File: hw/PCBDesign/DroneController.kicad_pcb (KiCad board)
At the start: 2 copper layers, 180 parts, among them J1 SerialDebug, J10 Conn_01x03, J11 Conn_01x03, J12 Conn_01x03, J13 Conn_01x03, J14 Conn_01x03, J2 USB_B_Micro, J3 ExtBatt, J4 Conn_ARM_JTAG_SWD_10, J5 EncoderConn, J6 JoystickConn, J7 Conn_01x03, J8 Conn_01x03, J9 Conn_01x03, Q1 MMBT3904, SW13 Key_User, SW15 Key_nRESET, SW17 Key_nBOOT, U1 74HC165, U10 AMS1117-3.3, U11 74HC595, U12 74HC595, U13 STM32F446RETx, U2 74HC165, U3 74HC165, U4 AT25SF081, U5 AT24C256, U6 NRF24L01_Breakout, U7 BQ24074RGT, U8 AMS1117-3.3, U9 AMS1117-3.3, Y1 8MHz Crystal

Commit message: Update pcb
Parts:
- added H1: MountingHole_Pad, MountingHole:MountingHole_3.2mm_M3_Pad_Via, F.Cu at (113.8, 83.8)
- added H2: MountingHole_Pad, MountingHole:MountingHole_3.2mm_M3_Pad_Via, F.Cu at (113.8, 126.0)
- added H3: MountingHole_Pad, MountingHole:MountingHole_3.2mm_M3_Pad_Via, F.Cu at (206.2, 83.8)
- added H4: MountingHole_Pad, MountingHole:MountingHole_3.2mm_M3_Pad_Via, F.Cu at (206.2, 126.0)
- J10, J11, J12, J13, J14, J5, J6, J7, J8, J9: moved to B.Cu
- moved D4 201.3 mm to (206.0, 97.8), turned to 180 degrees
- moved J10 193.1 mm to (170.8, 34.8)
- moved J11 193.1 mm to (195.3, 34.8)
- moved J13 193.1 mm to (183.0, 34.8)
- moved J8 193.1 mm to (158.5, 34.8)
- moved U6 191.0 mm to (155.0, 127.0), turned to 90 degrees
- moved SW15 189.9 mm to (205.7, 117.3)
- moved SW17 189.6 mm to (205.7, 111.8)
- moved D3 188.0 mm to (206.0, 100.3), turned to 180 degrees
- moved D5 183.6 mm to (206.0, 95.2), turned to 180 degrees
- moved D6 181.6 mm to (206.0, 92.7), turned to 180 degrees
- moved SW13 181.4 mm to (205.7, 106.2)
- moved J7 172.2 mm to (131.0, 49.0)
- moved J3 170.8 mm to (129.5, 86.4)
- moved J2 164.8 mm to (112.0, 105.0), turned to 270 degrees
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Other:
- board outline added: 100 x 50 mm

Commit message: Laid out power section
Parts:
- added R52: 33, Resistor_SMD:R_0402_1005Metric, F.Cu at (183.7, 148.6)
- added R54: 33, Resistor_SMD:R_0402_1005Metric, F.Cu at (186.6, 148.6)
- J10: value Conn_01x03 -> SW_B
- J11: value Conn_01x03 -> YTrim; moved to F.Cu
- J12: value Conn_01x03 -> SW_C
- J13: value Conn_01x03 -> TTrim; moved to F.Cu
- J14: value Conn_01x03 -> SW_D
- J6: moved to F.Cu
- J7: value Conn_01x03 -> PTrim; moved to F.Cu
- J8: value Conn_01x03 -> SW_A
- J9: value Conn_01x03 -> RTrim; moved to F.Cu
- moved U1 310.6 mm to (271.6, 106.4)
- moved U2 291.2 mm to (257.6, 119.2)
- moved U3 271.8 mm to (249.0, 106.4)
- moved C1 266.9 mm to (232.4, 116.5)
- moved C2 266.9 mm to (235.2, 116.5)
- moved R2 266.9 mm to (226.6, 118.5)
- moved R45 266.9 mm to (229.5, 118.5)
- moved R46 266.9 mm to (229.5, 116.5)
- moved R47 266.9 mm to (223.7, 118.5)
- moved R49 266.9 mm to (226.6, 116.5)
- moved R51 266.9 mm to (223.7, 116.5)
- moved C3 238.7 mm to (219.4, 109.6)
- moved R1 238.7 mm to (219.4, 107.6)
- moved C50 221.0 mm to (248.0, 95.6)
- moved Q1 221.0 mm to (223.3, 108.5)
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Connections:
- net Net-(C39-Pad1) renamed /Power Supply/VBattProtectOut
- R73 pad 2: +3V3 -> /Power Supply/vBatt
- R82 pad 2: +3V3 -> /Power Supply/vBatt
- R83 pad 2: +3V3 -> /Power Supply/vBatt
- U13 pad 44: /Power Supply/USB_D- -> Net-(R52-Pad2)
- U13 pad 45: /Power Supply/USB_D+ -> Net-(R54-Pad2)
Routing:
- net GND: track 0.00 -> 51.3 mm, vias 0 -> 26
- net /Power Supply/USB_D-: track 0.00 -> 26.3 mm
- net /Power Supply/USB_D+: track 0.00 -> 26.1 mm
- net /Power Supply/vBatt: track 0.00 -> 20.5 mm
- net /Power Supply/VBattProtectOut: track 0.00 -> 12.0 mm, vias 0 -> 13
- net nBatteryChargeGood: track 0.00 -> 11.1 mm, vias 0 -> 2
- net +5V: track 0.00 -> 10.5 mm
- net nBatteryPowerGood: track 0.00 -> 9.02 mm, vias 0 -> 1
- net /Power Supply/CHG_nEN: track 0.00 -> 8.27 mm, vias 0 -> 1
- net +3.3VP: track 0.00 -> 6.57 mm
- net +3V3: track 0.00 -> 6.54 mm, vias 0 -> 6
- net +3.3VADC: track 0.00 -> 6.54 mm, vias 0 -> 6
- net /Processor/BattChgCfg0: track 0.00 -> 3.47 mm, vias 0 -> 1
- net Net-(R72-Pad1): track 0.00 -> 3.14 mm
- net Net-(R78-Pad1): track 0.00 -> 2.73 mm
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- added copper zone on F.Cu, net +3.3VADC
- added copper zone on F.Cu, net +3V3
- added copper zone on F.Cu, net /Power Supply/VBattProtectOut
- added copper zone on In2.Cu, net /Power Supply/VBattProtectOut
- added copper zone on In1.Cu, net GND
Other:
- copper layers 2 -> 4
- net class Default: via_dia 0.8 -> 0.4; via_drill 0.4 -> 0.3
- board text added: "DN"
- board text added: "GND"
- board text added: "HM-BT4052"
- board text added: "INT"
- board text added: "PDN"
- board text added: "RXD"
- board text added: "TXD"
- board text added: "VDD"
- board text added: "WKUP"

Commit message: Lay out more PCB
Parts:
- removed C42, C43, C45, C46: 1uF, Capacitor_SMD:C_0805_2012Metric
- removed C48, C49: 100n, Capacitor_SMD:C_0402_1005Metric
- removed R86, R87: 10k, Resistor_SMD:R_0402_1005Metric
- removed U10, U9: AMS1117-3.3, Package_TO_SOT_SMD:SOT-223-3_TabPin2
- added C26: 100n, Capacitor_SMD:C_0402_1005Metric, F.Cu at (157.3, 103.2)
- added C27: 100n, Capacitor_SMD:C_0402_1005Metric, F.Cu at (155.0, 110.1)
- added C29: 100n, Capacitor_SMD:C_0402_1005Metric, F.Cu at (168.3, 119.2)
- added C31: 100n, Capacitor_SMD:C_0402_1005Metric, F.Cu at (171.7, 119.2)
- added C33: 100n, Capacitor_SMD:C_0402_1005Metric, F.Cu at (161.7, 110.0)
- added C55: 100n, Capacitor_SMD:C_0402_1005Metric, F.Cu at (169.8, 101.5)
- added C56: 100n, Capacitor_SMD:C_0402_1005Metric, F.Cu at (178.8, 109.1)
- added C57: 100n, Capacitor_SMD:C_0402_1005Metric, F.Cu at (176.9, 114.5)
- added C58: 100n, Capacitor_SMD:C_0402_1005Metric, F.Cu at (200.8, 116.6)
- added C59: 10uF, Capacitor_SMD:C_0805_2012Metric, F.Cu at (203.1, 116.6)
- added D7: BT_ON, LED_SMD:LED_0603_1608Metric, F.Cu at (206.6, 116.6)
- added Q2: si2302, Package_TO_SOT_SMD:SOT-23, F.Cu at (203.1, 119.3)
- added Q3: si2302, Package_TO_SOT_SMD:SOT-23, F.Cu at (182.4, 116.9)
- added Q4: si2301, Package_TO_SOT_SMD:SOT-23, F.Cu at (206.5, 119.3)
- added Q5: si2301, Package_TO_SOT_SMD:SOT-23, F.Cu at (185.8, 116.9)
- added R100: 10k, Resistor_SMD:R_0402_1005Metric, F.Cu at (199.7, 116.6)
- added R101: 560, Resistor_SMD:R_0402_1005Metric, F.Cu at (208.9, 116.5)
- added R56: 10k, Resistor_SMD:R_0402_1005Metric, F.Cu at (200.8, 119.3)
- added R58: 10k, Resistor_SMD:R_0402_1005Metric, F.Cu at (180.2, 116.9)
- added R59: 10k, Resistor_SMD:R_0402_1005Metric, F.Cu at (208.9, 119.2)
- added R98: 10k, Resistor_SMD:R_0402_1005Metric, F.Cu at (188.0, 116.9)
- added R99: 10k, Resistor_SMD:R_0402_1005Metric, F.Cu at (147.6, 103.2)
- added U14: RN4871, RF_Module:Microchip_RN4871, F.Cu at (201.1, 110.0)
- moved U1 135.8 mm to (136.0, 99.8), turned to 90 degrees
- moved R67 103.2 mm to (147.6, 104.4)
- moved R92 100.9 mm to (162.9, 141.3)
- moved R61 97.1 mm to (147.3, 114.8), turned to 180 degrees
- moved U4 95.9 mm to (152.4, 105.5)
- moved R62 94.8 mm to (147.3, 112.6)
- moved R60 94.5 mm to (147.3, 115.9)
- moved C23 92.7 mm to (157.0, 94.4)
- moved R65 92.3 mm to (147.3, 111.5)
- moved R63 92.3 mm to (147.3, 113.7), turned to 180 degrees
- moved R68 90.5 mm to (157.8, 112.1), turned to 270 degrees
- moved R66 89.9 mm to (147.3, 110.4), turned to 180 degrees
- moved R69 89.3 mm to (156.7, 112.1), turned to 270 degrees
- moved R95 87.7 mm to (169.6, 140.9)
- moved R97 87.0 mm to (170.6, 119.2), turned to 270 degrees
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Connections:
- C34 pad 1: +3.3VP -> Net-(C34-Pad1)
- C35 pad 1: +3.3VP -> Net-(C34-Pad1)
- J2 pad 4: Net-(J2-Pad4) -> (no net)
- J4 pad 7: Net-(J4-Pad7) -> (no net)
- R13 pad 1: /Human Machine Interface/d1 -> (no net)
- R14 pad 1: /Human Machine Interface/d0 -> (no net)
- R16 pad 2: /Human Machine Interface/d16 -> (no net)
- R18 pad 1: /Human Machine Interface/d8 -> (no net)
- R19 pad 2: /Human Machine Interface/d9 -> (no net)
- R2 pad 1: /Human Machine Interface/d23 -> (no net)
- R21 pad 2: /Human Machine Interface/d17 -> (no net)
- R25 pad 1: /Human Machine Interface/d10 -> (no net)
- R26 pad 2: /Human Machine Interface/d11 -> (no net)
- R27 pad 2: /Human Machine Interface/d18 -> (no net)
- R31 pad 1: /Human Machine Interface/d12 -> (no net)
- R32 pad 2: /Human Machine Interface/d13 -> (no net)
- R33 pad 2: /Human Machine Interface/d19 -> (no net)
- R37 pad 1: /Human Machine Interface/d14 -> (no net)
- R38 pad 2: /Human Machine Interface/d15 -> (no net)
- R45 pad 1: /Human Machine Interface/d22 -> (no net)
- R46 pad 1: /Human Machine Interface/d4 -> (no net)
- R47 pad 1: /Human Machine Interface/d5 -> (no net)
- R48 pad 2: /Human Machine Interface/d2 -> (no net)
- R49 pad 1: /Human Machine Interface/d6 -> (no net)
- R51 pad 1: /Human Machine Interface/d7 -> (no net)
- R55 pad 2: /Human Machine Interface/d3 -> (no net)
- R70 pad 1: +3.3VP -> Net-(C34-Pad1)
- R71 pad 1: +3.3VP -> Net-(C34-Pad1)
- U1 pad 11: /Human Machine Interface/d16 -> (no net)
- U1 pad 12: /Human Machine Interface/d17 -> (no net)
- U1 pad 13: /Human Machine Interface/d18 -> (no net)
- U1 pad 14: /Human Machine Interface/d19 -> (no net)
- U1 pad 3: nBatteryPowerGood -> (no net)
- U1 pad 4: nBatteryChargeGood -> (no net)
- U1 pad 5: /Human Machine Interface/d22 -> (no net)
- U1 pad 6: /Human Machine Interface/d23 -> (no net)
- U1 pad 7: Net-(U1-Pad7) -> (no net)
- U11 pad 1: /Processor/BattChgCfg1 -> (no net)
- U11 pad 15: /Processor/BattChgCfg0 -> (no net)
- U11 pad 2: /Power Supply/CHG_nEN -> (no net)
- U11 pad 3: /Processor/BT_nWakeup -> (no net)
- U11 pad 4: /Processor/BT_nPowerUp -> (no net)
- U11 pad 5: /Processor/BT_VCC_EN -> (no net)
- U11 pad 6: /Processor/RF24_VCC_EN -> (no net)
- U11 pad 9: Net-(U11-Pad9) -> (no net)
- U12 pad 1: Net-(U12-Pad1) -> (no net)
- U12 pad 15: Net-(U12-Pad15) -> (no net)
- U12 pad 2: Net-(U12-Pad2) -> (no net)
- U12 pad 3: Net-(U12-Pad3) -> (no net)
- U12 pad 9: Net-(U12-Pad9) -> (no net)
- U13 pad 13: +3.3VADC -> +3V3
- U13 pad 14: /Power Supply/V_Batt_Sense -> (no net)
- U13 pad 16: +3.3VP -> (no net)
- U13 pad 17: +3.3VADC -> (no net)
- U13 pad 2: Net-(U13-Pad2) -> (no net)
- U13 pad 28: Net-(U13-Pad28) -> (no net)
- U13 pad 3: Net-(U13-Pad3) -> (no net)
- U13 pad 39: /Wireless/BT_INT_REQ -> (no net)
- U13 pad 4: Net-(U13-Pad4) -> (no net)
- U13 pad 59: Net-(U13-Pad59) -> (no net)
- U2 pad 11: /Human Machine Interface/d8 -> (no net)
- U2 pad 12: /Human Machine Interface/d9 -> (no net)
- U2 pad 13: /Human Machine Interface/d10 -> (no net)
- U2 pad 14: /Human Machine Interface/d11 -> (no net)
- U2 pad 3: /Human Machine Interface/d12 -> (no net)
- U2 pad 4: /Human Machine Interface/d13 -> (no net)
- U2 pad 5: /Human Machine Interface/d14 -> (no net)
- U2 pad 6: /Human Machine Interface/d15 -> (no net)
- U2 pad 7: Net-(U2-Pad7) -> (no net)
- U3 pad 11: /Human Machine Interface/d0 -> (no net)
- U3 pad 12: /Human Machine Interface/d1 -> (no net)
- U3 pad 13: /Human Machine Interface/d2 -> (no net)
- U3 pad 14: /Human Machine Interface/d3 -> (no net)
- U3 pad 3: /Human Machine Interface/d4 -> (no net)
- U3 pad 4: /Human Machine Interface/d5 -> (no net)
- U3 pad 5: /Human Machine Interface/d6 -> (no net)
- U3 pad 6: /Human Machine Interface/d7 -> (no net)
- U3 pad 7: Net-(U3-Pad7) -> (no net)
- U6 pad 2: +3.3VP -> Net-(C34-Pad1)
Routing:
- net GND: track 51.3 -> 100.3 mm, vias 26 -> 68
- net +3V3: track 6.54 -> 54.3 mm, vias 6 -> 32
- net /Wireless/BT_TX: track 0.00 -> 33.3 mm, vias 0 -> 2
- net /Wireless/BT_RX: track 0.00 -> 32.3 mm, vias 0 -> 2
- net /Processor/RF24_nCS: track 0.00 -> 24.8 mm
- net /Processor/NOR_nCS: track 0.00 -> 23.8 mm, vias 0 -> 2
- net /Processor/NOR_MISO: track 0.00 -> 20.8 mm, vias 0 -> 2
- net /Processor/EEPROM_SDA: track 0.00 -> 20.5 mm, vias 0 -> 2
- net /Processor/EEPROM_SCL: track 0.00 -> 17.8 mm, vias 0 -> 2
- net /Human Machine Interface/ENC1_A: track 0.00 -> 17.7 mm
- net /Processor/RF24_nIRQ: track 0.00 -> 16.9 mm
- net /Human Machine Interface/ENC1_B: track 0.00 -> 16.2 mm
- net /Power Supply/USB_D+: track 26.1 -> 42.1 mm
- net /Power Supply/USB_D-: track 26.3 -> 42.2 mm
- net /Processor/NOR_SCK: track 0.00 -> 15.6 mm, vias 0 -> 2
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- added copper zone on In2.Cu, net +3V3
- removed copper zone on F.Cu, net +3.3VADC
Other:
- net class Default: clearance 0.2 -> 0.09
- rule trace_clearance: 0.2 -> 0.09
- board text removed: "DN"
- board text removed: "GND"
- board text removed: "HM-BT4052"
- board text removed: "INT"
- board text removed: "PDN"
- board text removed: "RXD"
- board text removed: "TXD"
- board text removed: "VDD"
- board text removed: "WKUP"

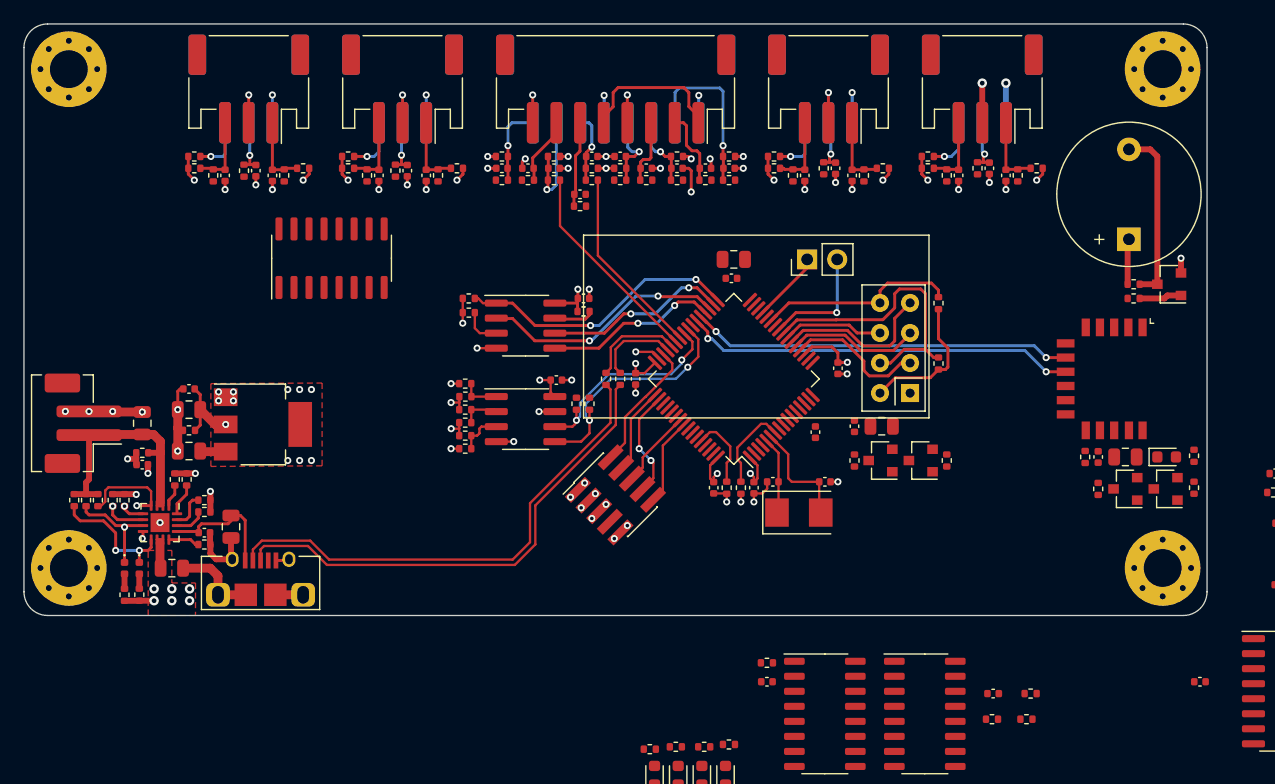
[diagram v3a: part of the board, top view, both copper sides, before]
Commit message: Routed most of the core peripherals
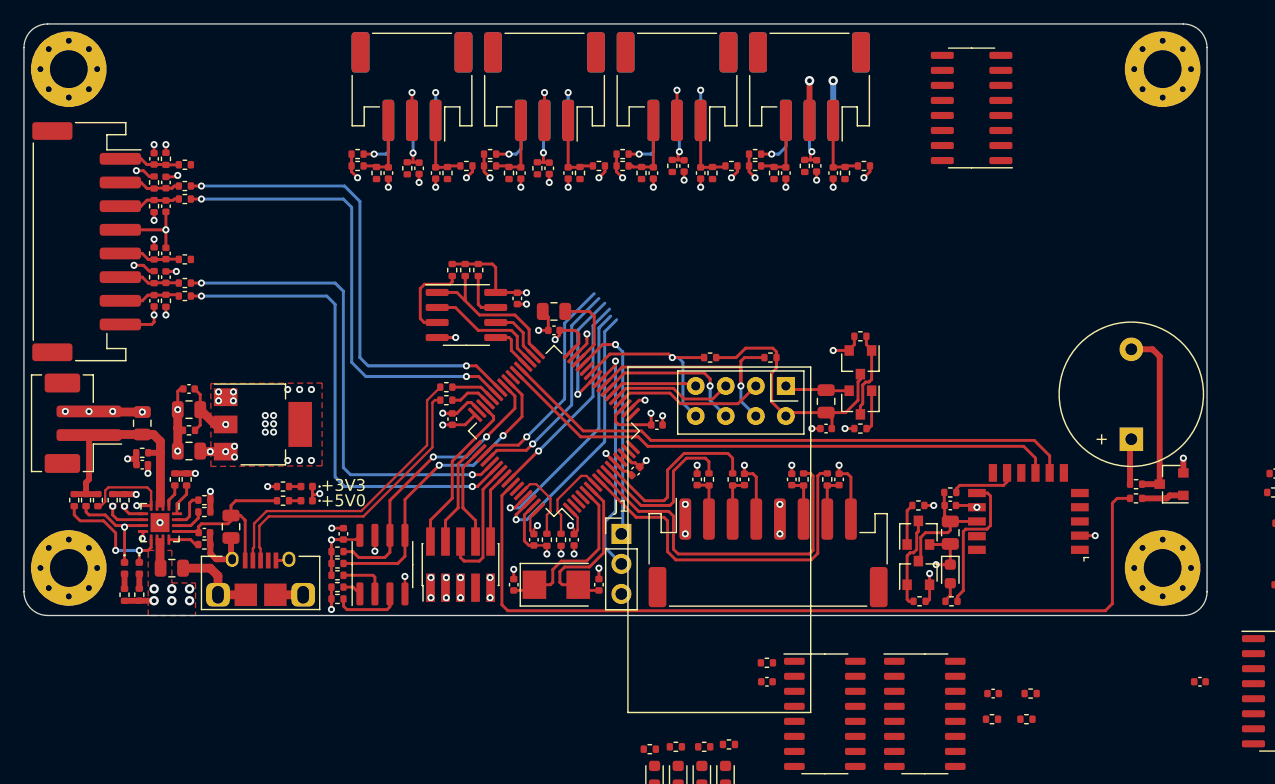
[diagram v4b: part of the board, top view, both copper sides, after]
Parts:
- removed R65: 10k, Resistor_SMD:R_0402_1005Metric
- added D8: LED_5V0, LED_SMD:LED_0402_1005Metric, F.Cu at (133.9, 120.3)
- added D9: LED_3V3, LED_SMD:LED_0402_1005Metric, F.Cu at (133.9, 119.1)
- J1: footprint Connector_PinHeader_2.54mm:PinHeader_1x02_P2.54mm_Vertical -> Connector_PinHeader_2.54mm:PinHeader_1x03_P2.54mm_Vertical
- J5: moved to F.Cu
- R60: value 10k -> 1.5k
- R63: value 10k -> 330
- moved U1 55.6 mm to (190.1, 87.1), turned to 180 degrees
- moved C7 49.9 mm to (121.0, 103.4), turned to 270 degrees
- moved R10 49.1 mm to (122.0, 103.4), turned to 270 degrees
- moved R6 47.0 mm to (123.6, 103.0)
- moved J5 46.6 mm to (115.3, 98.4), turned to 270 degrees
- moved R9 45.4 mm to (121.0, 101.4), turned to 270 degrees
- moved C6 44.2 mm to (122.0, 101.4), turned to 270 degrees
- moved R5 42.5 mm to (123.6, 101.9)
- moved J6 41.3 mm to (172.9, 124.7), turned to 0 degrees
- moved R12 40.1 mm to (121.0, 99.4), turned to 270 degrees
- moved C9 39.3 mm to (122.0, 99.4), turned to 90 degrees
- moved R14 37.4 mm to (123.6, 99.9), turned to 180 degrees
- moved C22 37.2 mm to (178.9, 118.5), turned to 90 degrees
- moved R8 37.1 mm to (121.0, 95.4), turned to 270 degrees
- moved C5 36.2 mm to (122.0, 95.4), turned to 270 degrees
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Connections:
- J6 pad 1: /Human Machine Interface/VAnalogRef -> +3V3
- J6 pad 5: /Human Machine Interface/VAnalogRef -> +3V3
- R60 pad 1: +3V3 -> Net-(D8-Pad2)
- R60 pad 2: Net-(R60-Pad2) -> +5V
- R61 pad 1: Net-(R60-Pad2) -> Net-(R61-Pad1)
- R63 pad 1: Net-(R62-Pad2) -> Net-(D9-Pad2)
- R63 pad 2: GND -> +3V3
- R66 pad 1: Net-(R65-Pad2) -> GND
- R66 pad 2: GND -> Net-(R66-Pad2)
- U13 pad 10: /Processor/ANALOG_IN_VYAW -> /Processor/ANALOG_IN_VTHROTTLE
- U13 pad 11: /Processor/ANALOG_IN_VTHROTTLE -> /Processor/ANALOG_IN_VYAW
- U13 pad 14: (no net) -> +3V3
- U13 pad 15: +3V3 -> (no net)
- U13 pad 42: /Human Machine Interface/ENC1_B -> /Human Machine Interface/ENC1_A
- U13 pad 43: /Human Machine Interface/ENC1_A -> /Human Machine Interface/ENC1_B
- U13 pad 53: /Human Machine Interface/ENC0_B -> /Human Machine Interface/ENC0_A
- U13 pad 54: /Human Machine Interface/ENC0_A -> /Human Machine Interface/ENC0_B
- U13 pad 8: /Processor/ANALOG_IN_VPITCH -> /Processor/ANALOG_IN_VROLL
- U13 pad 9: /Processor/ANALOG_IN_VROLL -> /Processor/ANALOG_IN_VPITCH
- U5 pad 1: Net-(R65-Pad2) -> Net-(R66-Pad2)
- U5 pad 3: Net-(R60-Pad2) -> Net-(R61-Pad1)
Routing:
- net /Human Machine Interface/PWM_Buzzer: track 0.00 -> 72.7 mm
- net /Human Machine Interface/ENC0_B: track 0.00 -> 41.7 mm, vias 0 -> 2
- net /Human Machine Interface/ENC0_A: track 0.00 -> 41.3 mm, vias 0 -> 2
- net GND: track 100.3 -> 139.3 mm, vias 68 -> 75
- net /Processor/ANALOG_IN_VROLL: track 0.00 -> 30.4 mm
- net /Processor/ANALOG_IN_VPITCH: track 0.00 -> 29.4 mm
- net /Human Machine Interface/ENC1_B: track 16.2 -> 40.3 mm, vias 0 -> 2
- net /Human Machine Interface/ENC1_A: track 17.7 -> 41.0 mm, vias 0 -> 2
- net /Human Machine Interface/KEY_nCS: track 0.00 -> 23.0 mm, vias 0 -> 1
- net /Human Machine Interface/KEY_nSAMPLE: track 0.00 -> 21.8 mm, vias 0 -> 1
- net +3V3: track 54.3 -> 74.0 mm, vias 32 -> 45
- net /Human Machine Interface/KEY_MISO: track 0.00 -> 19.0 mm, vias 0 -> 1
- net /Human Machine Interface/KEY_SCK: track 0.00 -> 18.8 mm, vias 0 -> 1
- net /Processor/KeyOut_nCS: track 0.00 -> 18.1 mm, vias 0 -> 1
- net /Power Supply/USB_D+: track 42.1 -> 24.9 mm
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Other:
- board text added: "+3V3"
- board text added: "+5V0"

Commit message: Complete route of draft #1 finished
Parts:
- removed C51: 100n, Capacitor_SMD:C_0402_1005Metric
- removed D3: DBG_LED_3, LED_SMD:LED_0603_1608Metric
- removed R89, R91: 10k, Resistor_SMD:R_0402_1005Metric
- removed R92: 560, Resistor_SMD:R_0402_1005Metric
- removed U12: 74HC595, Package_SO:SO-16_3.9x9.9mm_P1.27mm
- moved U3 93.5 mm to (131.0, 98.4)
- moved SW17 88.0 mm to (125.0, 84.0)
- moved C3 85.6 mm to (131.0, 92.7), turned to 180 degrees
- moved R57 83.2 mm to (124.0, 87.5)
- moved R55 82.2 mm to (126.0, 88.6)
- moved C32 80.8 mm to (126.0, 87.5), turned to 180 degrees
- moved SW13 80.0 mm to (132.0, 84.0)
- moved R1 77.7 mm to (130.9, 104.3), turned to 180 degrees
- moved R48 73.7 mm to (133.0, 88.6)
- moved R50 73.6 mm to (131.0, 87.5)
- moved C28 73.3 mm to (133.0, 87.5), turned to 180 degrees
- moved U2 68.0 mm to (154.0, 99.0), turned to 270 degrees
- moved R53 62.6 mm to (136.7, 112.0), turned to 90 degrees
- moved C2 62.1 mm to (159.8, 101.4), turned to 90 degrees
- moved D4 61.7 mm to (208.0, 99.0), turned to 180 degrees
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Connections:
- R13 pad 1: (no net) -> /Human Machine Interface/d6
- R14 pad 1: (no net) -> /Human Machine Interface/d7
- R16 pad 2: (no net) -> /Human Machine Interface/d23
- R18 pad 1: (no net) -> /Human Machine Interface/d14
- R19 pad 2: (no net) -> /Human Machine Interface/d12
- R2 pad 1: (no net) -> /Human Machine Interface/d17
- R21 pad 2: (no net) -> /Human Machine Interface/d9
- R25 pad 1: (no net) -> /Human Machine Interface/d3
- R26 pad 2: (no net) -> /Human Machine Interface/d15
- R27 pad 2: (no net) -> /Human Machine Interface/d13
- R31 pad 1: (no net) -> /Human Machine Interface/d8
- R32 pad 2: (no net) -> /Human Machine Interface/d10
- R33 pad 2: (no net) -> /Human Machine Interface/d2
- R37 pad 1: (no net) -> /Human Machine Interface/d11
- R38 pad 2: (no net) -> /Human Machine Interface/d22
- R45 pad 1: (no net) -> /Human Machine Interface/d21
- R46 pad 1: (no net) -> /Human Machine Interface/d20
- R47 pad 1: (no net) -> /Human Machine Interface/d18
- R48 pad 2: (no net) -> /Human Machine Interface/d4
- R49 pad 1: (no net) -> /Human Machine Interface/d16
- R51 pad 1: (no net) -> /Human Machine Interface/d19
- R55 pad 2: (no net) -> /Human Machine Interface/d5
- U1 pad 11: (no net) -> /Human Machine Interface/d16
- U1 pad 12: (no net) -> /Human Machine Interface/d17
- U1 pad 13: (no net) -> /Human Machine Interface/d18
- U1 pad 14: (no net) -> /Human Machine Interface/d19
- U1 pad 3: (no net) -> /Human Machine Interface/d20
- U1 pad 4: (no net) -> /Human Machine Interface/d21
- U1 pad 5: (no net) -> /Human Machine Interface/d22
- U1 pad 6: (no net) -> /Human Machine Interface/d23
- U11 pad 1: (no net) -> /Processor/BT_VCC_EN
- U11 pad 15: (no net) -> /Processor/RF24_VCC_EN
- U11 pad 2: (no net) -> /Processor/BattChgCfg0
- U11 pad 3: (no net) -> /Processor/BattChgCfg1
- U11 pad 4: (no net) -> /Power Supply/CHG_nEN
- U11 pad 5: (no net) -> Net-(R95-Pad2)
- U11 pad 6: (no net) -> Net-(R94-Pad2)
- U11 pad 7: Net-(U11-Pad7) -> Net-(R93-Pad2)
- U2 pad 11: (no net) -> /Human Machine Interface/d8
- U2 pad 12: (no net) -> /Human Machine Interface/d9
- U2 pad 13: (no net) -> /Human Machine Interface/d10
- U2 pad 14: (no net) -> /Human Machine Interface/d11
- U2 pad 3: (no net) -> /Human Machine Interface/d12
- U2 pad 4: (no net) -> /Human Machine Interface/d13
- U2 pad 5: (no net) -> /Human Machine Interface/d14
- U2 pad 6: (no net) -> /Human Machine Interface/d15
- U3 pad 11: (no net) -> nBatteryPowerGood
- U3 pad 12: (no net) -> nBatteryChargeGood
- U3 pad 13: (no net) -> /Human Machine Interface/d2
- U3 pad 14: (no net) -> /Human Machine Interface/d3
- U3 pad 3: (no net) -> /Human Machine Interface/d4
- U3 pad 4: (no net) -> /Human Machine Interface/d5
- U3 pad 5: (no net) -> /Human Machine Interface/d6
- U3 pad 6: (no net) -> /Human Machine Interface/d7
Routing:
- net /Human Machine Interface/KEY_SCK: track 18.8 -> 121.1 mm, vias 1 -> 5
- net /Processor/BattChgCfg0: track 3.47 -> 96.8 mm, vias 1 -> 2
- net /Power Supply/CHG_nEN: track 8.27 -> 101.6 mm, vias 1 -> 2
- net /Processor/BattChgCfg1: track 1.97 -> 94.8 mm, vias 1 -> 2
- net /Human Machine Interface/KEY_nSAMPLE: track 21.8 -> 105.7 mm, vias 1 -> 4
- net /Human Machine Interface/KEY_nCS: track 23.0 -> 82.7 mm, vias 1 -> 4
- net GND: track 139.3 -> 188.4 mm, vias 75 -> 88
- net nBatteryChargeGood: track 11.1 -> 52.5 mm
- net Net-(U1-Pad10): track 0.00 -> 40.3 mm, vias 0 -> 2
- net nBatteryPowerGood: track 9.02 -> 49.0 mm, vias 1 -> 0
- net /Human Machine Interface/nRESET: track 7.33 -> 44.5 mm, vias 0 -> 2
- net /Processor/BT_VCC_EN: track 3.48 -> 37.5 mm
- net /Processor/KeyOut_nCS: track 18.1 -> 45.6 mm, vias 1 -> 2
- net /Processor/KEY_MOSI: track 10.7 -> 35.8 mm, vias 1 -> 2
- net /Human Machine Interface/d11: track 0.00 -> 24.7 mm
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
